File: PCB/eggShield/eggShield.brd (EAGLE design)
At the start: 51.3 x 53.3 mm, 54 parts, among them J2 AVR_SPI_PRG_6NS, U1 V_REG_LDOSMD, U2 V_REG_LDOSMD, U3 MCP42XXX

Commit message: picked a more direct route for the 2.5v bug fix
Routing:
- net 5V: track 272.5 -> 268.9 mm, vias 9 -> 8
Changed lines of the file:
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@@
 <wire x1="33.362" y1="26.289" x2="34.857" y2="26.289" width="0.6096" layer="1"/>
 <wire x1="34.857" y1="26.289" x2="34.991" y2="26.155" width="0.6096" layer="1"/>
-<wire x1="29.083" y1="20.701" x2="29.083" y2="27.051" width="0.6096" layer="16"/>
-<wire x1="29.083" y1="27.051" x2="30.226" y2="28.194" width="0.6096" layer="16"/>
-<wire x1="30.226" y1="28.194" x2="33.3375" y2="28.194" width="0.6096" layer="16"/>
-<via x="33.3375" y="28.194" extent="1-16" drill="0.3302"/>
-<wire x1="33.3375" y1="28.194" x2="33.362" y2="28.1695" width="0.6096" layer="1"/>
-<wire x1="33.362" y1="28.1695" x2="33.362" y2="26.289" width="0.6096" layer="1"/>
+<wire x1="28.321" y1="32.131" x2="28.321" y2="31.1785" width="0.6096" layer="1"/>
+<wire x1="30.2895" y1="28.194" x2="32.766" y2="28.194" width="0.6096" layer="1"/>
+<wire x1="32.766" y1="28.194" x2="33.401" y2="27.559" width="0.6096" layer="1"/>
+<wire x1="33.401" y1="27.559" x2="33.401" y2="26.328" width="0.6096" layer="1"/>
+<wire x1="33.401" y1="26.328" x2="33.362" y2="26.289" width="0.6096" layer="1"/>
+<wire x1="30.2895" y1="28.194" x2="29.337" y2="29.1465" width="0.6096" layer="1"/>
+<wire x1="29.337" y1="29.1465" x2="29.337" y2="30.1625" width="0.6096" layer="1"/>
+<wire x1="29.337" y1="30.1625" x2="28.321" y2="31.1785" width="0.6096" layer="1"/>
 </signal>
 <signal name="MOSI_B">

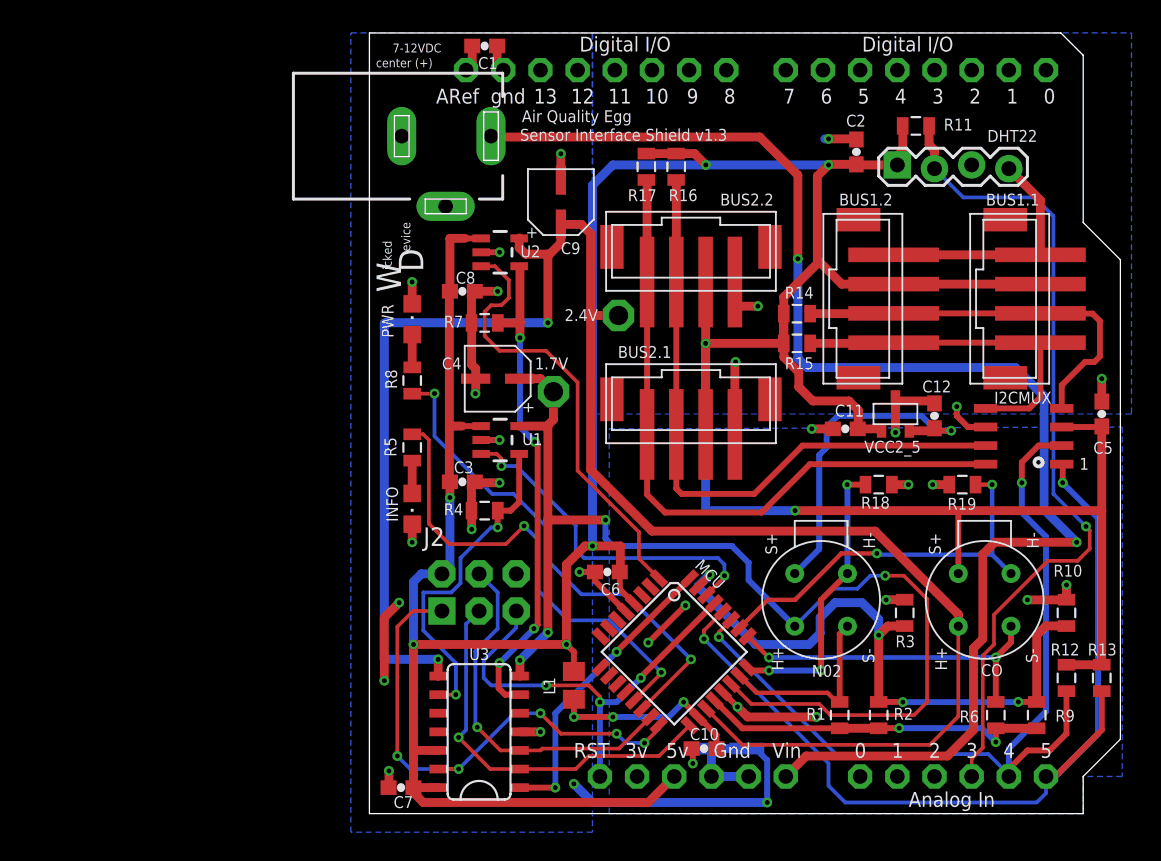
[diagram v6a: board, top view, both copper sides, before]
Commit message: updates to the initial prototype based on testing and feedback. Fixed crossed up digipot lines, rotated the DHT22, move the barrel jack off the headers, replaced 0603s with 0805s.
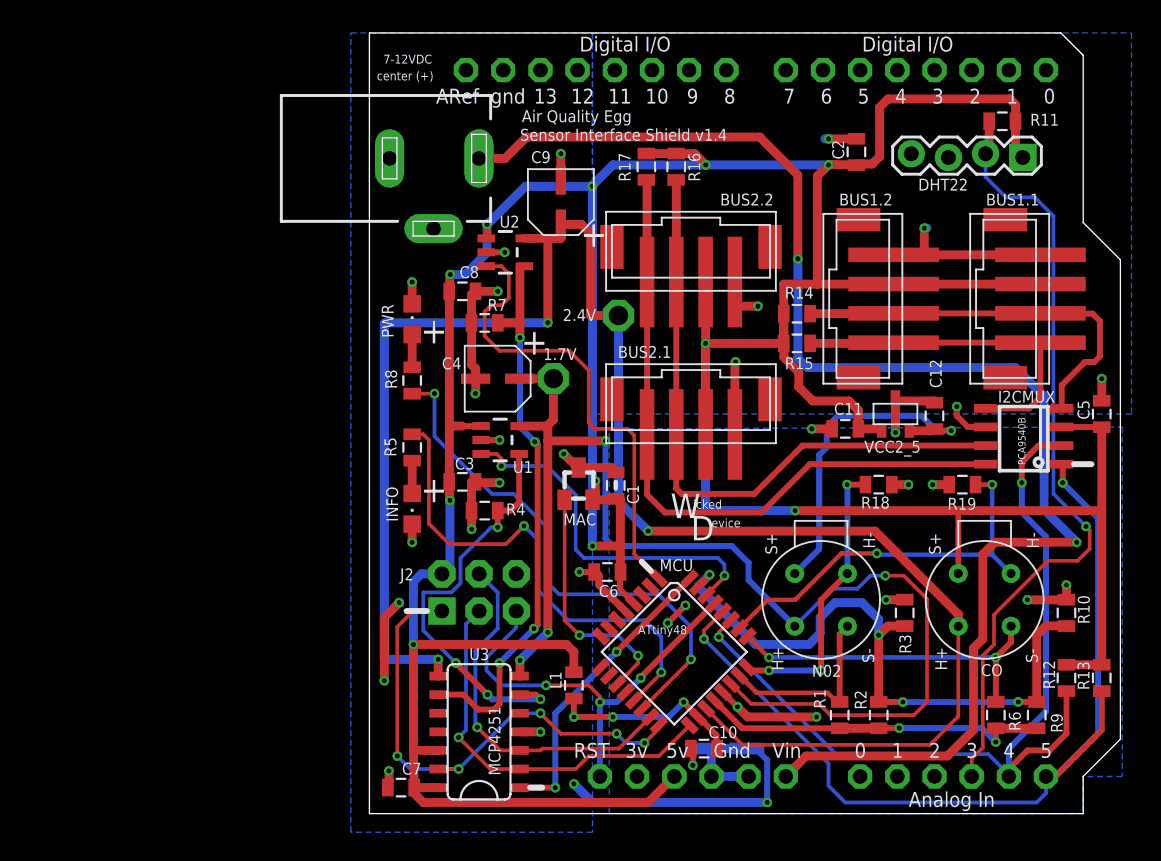
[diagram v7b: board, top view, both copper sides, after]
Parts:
- added MAC: 11AA02E48, nanode:SOT23
- C1, C10, C11, C12, C2, C3, C5, C6, C7, C8: device SparkFun:0603-CAP -> SparkFun-Passives:0805
- L1: device nanodeRF_11:RCL_R0805 -> SparkFun-Passives:0805
- moved C1 31.3 mm to (16.8, 22.4), turned to 90 degrees
- moved DHT22 8.61 mm to (44.6, 45.0), turned to 180 degrees
- moved R11 5.91 mm to (43.2, 47.3), turned to 180 degrees
- moved 7-12VDC 1.73 mm to (4.38, 44.8)
- moved TP1 0.89 mm to (12.6, 29.7)
- moved U2 0.36 mm to (9.29, 38.4)
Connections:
- removed net N$4: C1.2, U$7.AREF
- new net MAC_IO: MAC.1, MCU.11
- net 5V: now also C1.1, MAC.2
- net CO_RH-: now also U3.9; no longer U3.6
- net GND: now also 7-12VDC.2, C1.2, MAC.3; no longer C1.1
- net NO2_RH-: now also U3.6; no longer U3.9
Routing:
- net 5V: track 268.9 -> 291.2 mm, vias 8 -> 11
- net MAC_IO: track 0.00 -> 16.8 mm, vias 0 -> 2
- net NO2_HEATER_V: track 79.1 -> 85.1 mm
- net NO2_RH-: track 23.2 -> 28.2 mm, vias 2 -> 4
- net CO_RH-: track 33.6 -> 38.0 mm
- net DHT22_IO: track 56.4 -> 53.5 mm
- net POWER: track 34.3 -> 36.5 mm
- net CO_HEATER_EN: track 30.6 -> 32.7 mm
- net N$4: track 1.82 -> 0.00 mm
- net AGND: track 27.3 -> 25.5 mm
- net CO_HEATER_V: track 124.7 -> 123.2 mm, vias 2 -> 3
- net STATUS: track 32.9 -> 34.3 mm
- net VIN: track 96.5 -> 97.9 mm
- net NO2_HEATER_EN: track 23.6 -> 24.8 mm
- net /RESET: track 30.1 -> 29.5 mm
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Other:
- board text added: "+"
- board text added: "ATtiny48"
- board text added: "MCP4251"
- board text added: "PCA9540B"
- board text added: "Sensor Interface Shield v1.4"
- board text removed: "1"
- board text removed: "Sensor Interface Shield v1.3"
